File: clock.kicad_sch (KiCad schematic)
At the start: 54 parts, among them J1 USB_C_Receptacle_USB2.0_16P, J2 Conn_01x02_Pin, J3 Conn_01x02_Pin, J4 Conn_01x02_Pin, J5 Battery, Q1 2N7002K, Q2 NPN, SW1 SW_Push, SW2 SW_Push, SW3 SW_Push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

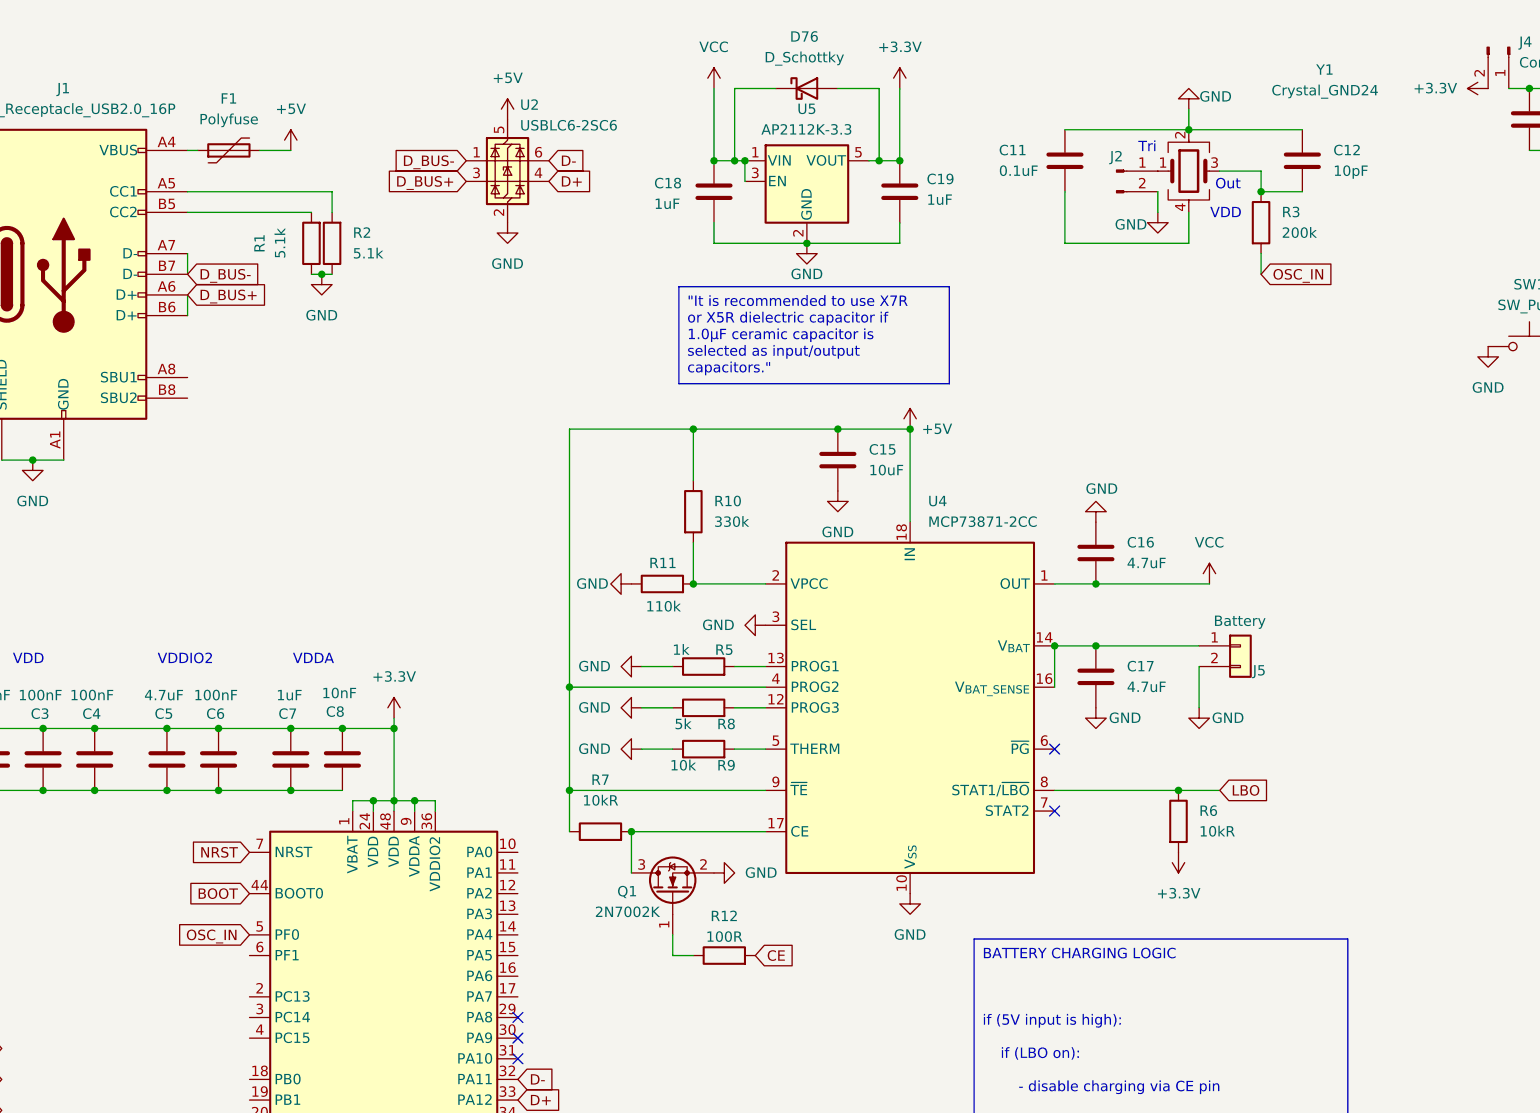
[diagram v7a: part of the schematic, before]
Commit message: started layout, redid the crystal
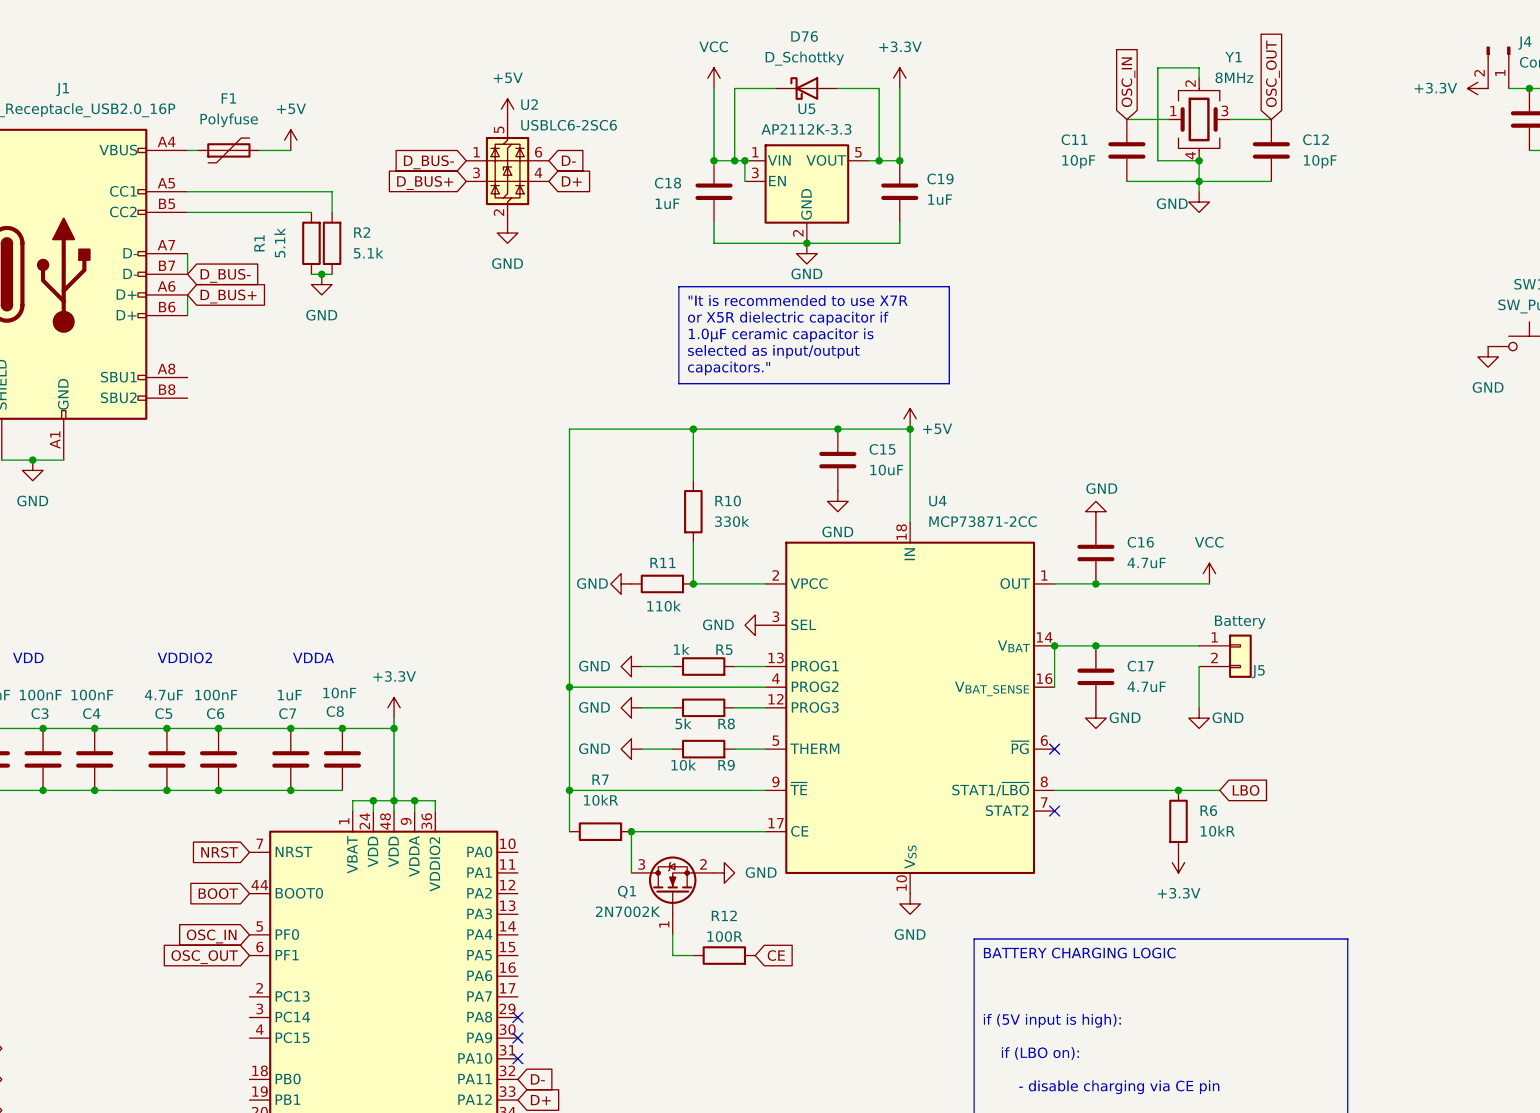
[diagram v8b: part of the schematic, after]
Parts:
- removed J2: Conn_01x02_Pin, Connector_PinHeader_2.54mm:PinHeader_1x02_P2.54mm_Vertical, symbol Connector:Conn_01x02_Pin
- removed R3: 200k, Resistor_SMD:R_0603_1608Metric_Pad0.98x0.95mm_HandSolder, symbol Device:R
- C11: value 0.1uF -> 10pF; footprint (none) -> Capacitor_SMD:C_0402_1005Metric_Pad0.74x0.62mm_HandSolder
- C12: footprint (none) -> Capacitor_SMD:C_0402_1005Metric_Pad0.74x0.62mm_HandSolder
- C16, C17: footprint (none) -> Capacitor_SMD:C_0805_2012Metric_Pad1.18x1.45mm_HandSolder
- Y1: value Crystal_GND24 -> 8MHz
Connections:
- net GND: now also C11.2, C12.2, Y1.4; no longer C11.1, C12.1
- net OSC_IN: now also C11.1, Y1.1
- net OSC_OUT: now reaches Y1.3
- net OSC_OUT: now also C12.1, U1.6 (PF1); no longer C12.2
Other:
- note removed: "Out"
- note removed: "Tri"
- moved on the sheet: C11, C12, Y1
